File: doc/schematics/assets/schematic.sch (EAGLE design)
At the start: 3 parts

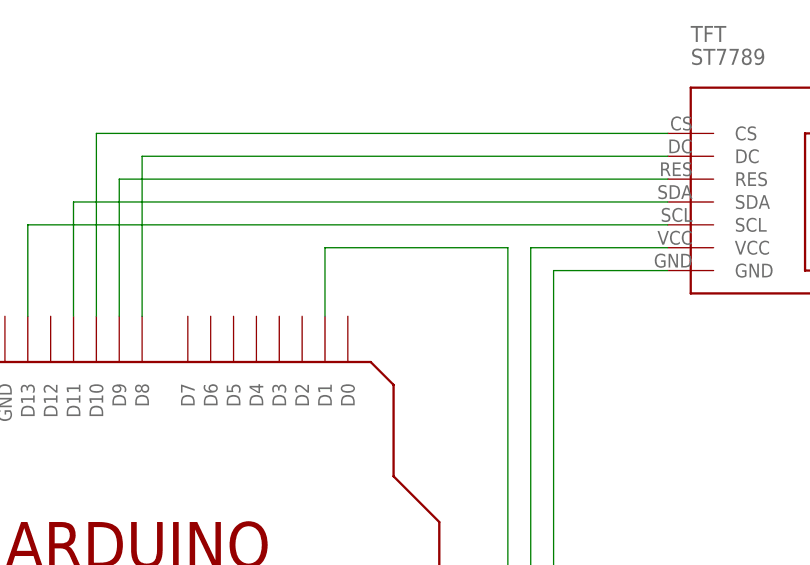
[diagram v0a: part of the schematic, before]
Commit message: fix: Wrong pin assignment of digital input pin in schematic
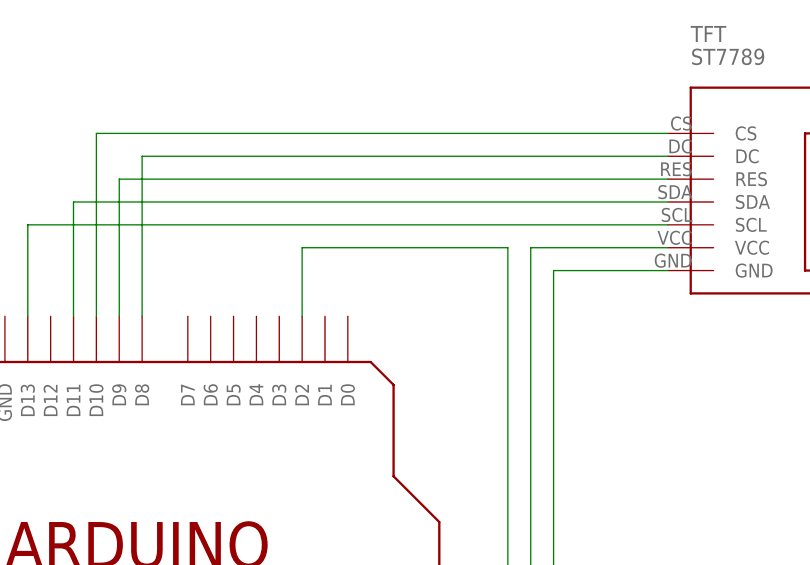
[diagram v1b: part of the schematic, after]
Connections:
- net N$6: now also ARDUINO_UNO_R3.D2; no longer ARDUINO_UNO_R3.D1
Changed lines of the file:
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@@
 <net name="N$6" class="0">
 <segment>
-<pinref part="ARDUINO_UNO_R3" gate="G$1" pin="D1"/>
-<wire x1="50.8" y1="66.04" x2="50.8" y2="73.66" width="0.1524" layer="91"/>
-<wire x1="50.8" y1="73.66" x2="71.12" y2="73.66" width="0.1524" layer="91"/>
+<wire x1="48.26" y1="73.66" x2="71.12" y2="73.66" width="0.1524" layer="91"/>
 <wire x1="71.12" y1="73.66" x2="71.12" y2="-10.16" width="0.1524" layer="91"/>
 <pinref part="JOYSTICK" gate="G$1" pin="SW"/>
 <wire x1="71.12" y1="-10.16" x2="88.9" y2="-10.16" width="0.1524" layer="91"/>
+<pinref part="ARDUINO_UNO_R3" gate="G$1" pin="D2"/>
+<wire x1="48.26" y1="66.04" x2="48.26" y2="73.66" width="0.1524" layer="91"/>
 </segment>
 </net>
